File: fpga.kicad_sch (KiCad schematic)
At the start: 29 parts, among them U201 ICE40HX4K, U202 W25Q16JV, U203 IS61WV25616FBLL-10TLI

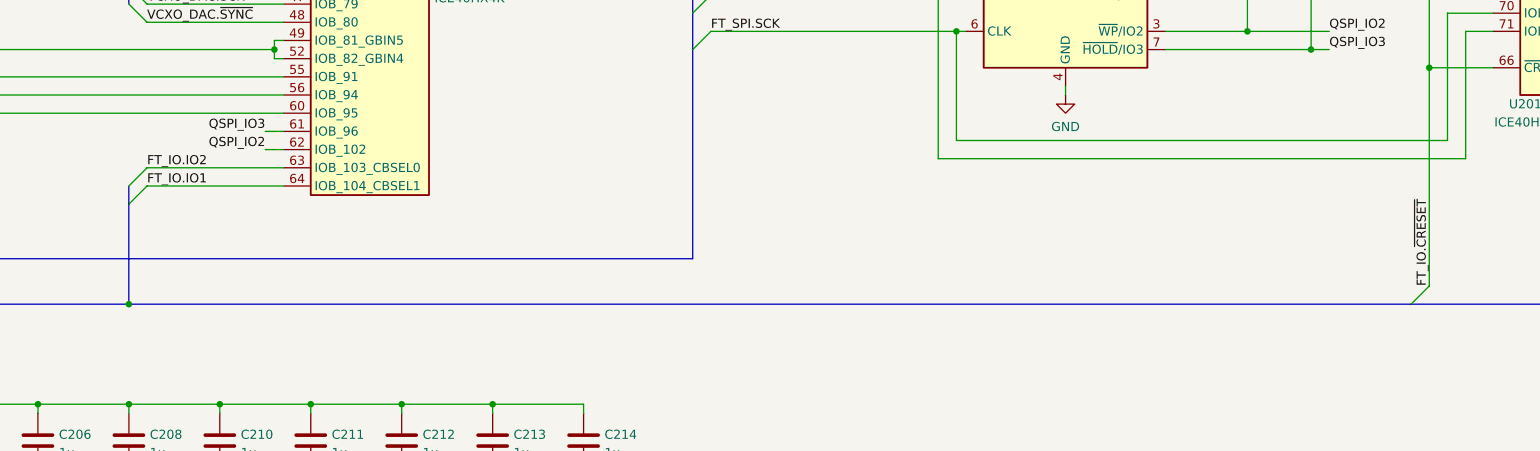
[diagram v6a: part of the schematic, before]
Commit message: Add testpoints for CDONE and CRESET
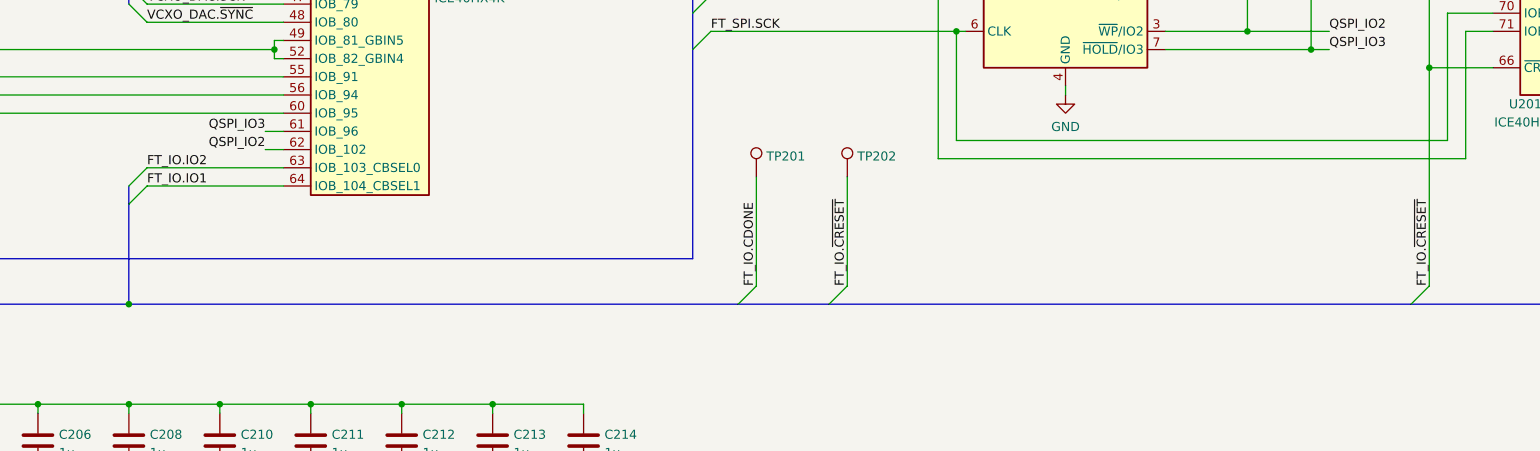
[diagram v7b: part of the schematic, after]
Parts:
- added TP201, TP202: TestPoint, TestPoint:TestPoint_THTPad_D1.0mm_Drill0.5mm, symbol Connector:TestPoint
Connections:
- net FT_IO.CDONE: now also TP201.1
- net FT_IO.~{CRESET}: now also TP202.1
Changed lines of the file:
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@@
     (stroke (width 0) (type default) (color 0 0 0 0))
   )
+  (bus_entry (at 212.09 222.25) (size 2.54 -2.54)
+    (stroke (width 0) (type default) (color 0 0 0 0))
+  )
   (bus_entry (at 350.52 222.25) (size 2.54 -2.54)
     (stroke (width 0) (type default) (color 0 0 0 0))
@@
     (stroke (width 0) (type default) (color 0 0 0 0))
   )
+  (bus_entry (at 224.79 222.25) (size 2.54 -2.54)
+    (stroke (width 0) (type default) (color 0 0 0 0))
+  )
   (bus_entry (at 256.54 82.55) (size -2.54 -2.54)
     (stroke (width 0) (type default) (color 0 0 0 0))
@@
     (stroke (width 0) (type default) (color 0 0 0 0))
   )
+  (bus (pts (xy 224.79 222.25) (xy 306.07 222.25))
+    (stroke (width 0) (type default) (color 0 0 0 0))
+  )
   (wire (pts (xy 177.8 236.22) (xy 177.8 237.49))
     (stroke (width 0) (type default) (color 0 0 0 0))
@@
     (stroke (width 0) (type default) (color 0 0 0 0))
   )
-  (bus (pts (xy 127 222.25) (xy 306.07 222.25))
+  (bus (pts (xy 127 222.25) (xy 212.09 222.25))
     (stroke (width 0) (type default) (color 0 0 0 0))
   )
@@
     (stroke (width 0) (type default) (color 0 0 0 0))
   )
+  (wire (pts (xy 214.63 204.47) (xy 214.63 219.71))
+    (stroke (width 0) (type default) (color 0 0 0 0))
+  )
   (bus (pts (xy 133.35 69.85) (xy 133.35 72.39))
     (stroke (width 0) (type default) (color 0 0 0 0))
@@
     (stroke (width 0) (type default) (color 0 0 0 0))
   )
+  (bus (pts (xy 212.09 222.25) (xy 224.79 222.25))
+    (stroke (width 0) (type default) (color 0 0 0 0))
+  )
   (wire (pts (xy 193.04 125.73) (xy 212.09 125.73))
     (stroke (width 0) (type default) (color 0 0 0 0))
@@
     (stroke (width 0) (type default) (color 0 0 0 0))
   )
+  (wire (pts (xy 227.33 204.47) (xy 227.33 219.71))
+    (stroke (width 0) (type default) (color 0 0 0 0))
+  )
   (wire (pts (xy 199.39 85.09) (xy 212.09 85.09))
     (stroke (width 0) (type default) (color 0 0 0 0))
@@
     (effects (font (size 1.27 1.27)) (justify left bottom))
   )
+  (label "FT_IO.CDONE" (at 214.63 219.71 90)
+    (effects (font (size 1.27 1.27)) (justify left bottom))
+  )
   (label "FT_SPI.~{CS}" (at 208.28 179.07 0)
     (effects (font (size 1.27 1.27)) (justify left bottom))
@@
     (effects (font (size 1.27 1.27)) (justify left bottom))
   )
+  (label "FT_IO.~{CRESET}" (at 227.33 219.71 90)
+    (effects (font (size 1.27 1.27)) (justify left bottom))
+  )
   (label "SRAM.A2" (at 313.69 68.58 0)
     (effects (font (size 1.27 1.27)) (justify left bottom))
@@
     (pin "1")
   )
+  (symbol (lib_id "Connector:TestPoint") (at 214.63 204.47 0) (unit 1)
+    (in_bom yes) (on_board yes) (fields_autoplaced)
+    (property "Reference" "TP201" (id 0) (at 216.027 201.6018 0)
+      (effects (font (size 1.27 1.27)) (justify left))
+    )
+    (property "Value" "TestPoint" (id 1) (at 216.027 203.0346 0)
+      (effects (font (size 1.27 1.27)) (justify left) hide)
+    )
+    (property "Footprint" "TestPoint:TestPoint_THTPad_D1.0mm_Drill0.5mm" (id 2) (at 219.71 204.47 0)
+      (effects (font (size 1.27 1.27)) hide)
+    )
+    (property "Datasheet" "~" (id 3) (at 219.71 204.47 0)
+      (effects (font (size 1.27 1.27)) hide)
+    )
+    (pin "1")
+  )
   (symbol (lib_id "symbols:+3.3VD") (at 161.29 40.64 0) (unit 1)
     (in_bom yes) (on_board yes) (fields_autoplaced)
@@
     (pin "2")
   )
+  (symbol (lib_id "Connector:TestPoint") (at 227.33 204.47 0) (unit 1)
+    (in_bom yes) (on_board yes) (fields_autoplaced)
+    (property "Reference" "TP202" (id 0) (at 228.727 201.6018 0)
+      (effects (font (size 1.27 1.27)) (justify left))
+    )
+    (property "Value" "TestPoint" (id 1) (at 228.727 203.0346 0)
+      (effects (font (size 1.27 1.27)) (justify left) hide)
+    )
+    (property "Footprint" "TestPoint:TestPoint_THTPad_D1.0mm_Drill0.5mm" (id 2) (at 232.41 204.47 0)
+      (effects (font (size 1.27 1.27)) hide)
+    )
+    (property "Datasheet" "~" (id 3) (at 232.41 204.47 0)
+      (effects (font (size 1.27 1.27)) hide)
+    )
+    (pin "1")
+  )
   (symbol (lib_id "Device:C_Polarized") (at 379.73 154.94 0) (unit 1)
